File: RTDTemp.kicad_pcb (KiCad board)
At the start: 2 copper layers, 92 parts, among them J1 Conn_01x04, J10 Conn_01x04, J11 Conn_01x02, J2 Conn_01x04, J3 Conn_01x04, J4 CAN_In, J5 CAN_Out, J6 Conn_01x04, J7 Conn_01x04, J8 Conn_01x04, J9 Conn_01x04, U1 MAX31865xAP, U10 MAX31865xAP, U11 MAX31865xAP, U12 MAX31865xAP, U2 Nucleo_L432KC, U3 PDS1-Sx-Sx, U4 MAX31865xAP, U5 ADM3055E, U6 MAX31865xAP, U7 CDSOT23-T24CAN, U8 MAX31865xAP, U9 MAX31865xAP

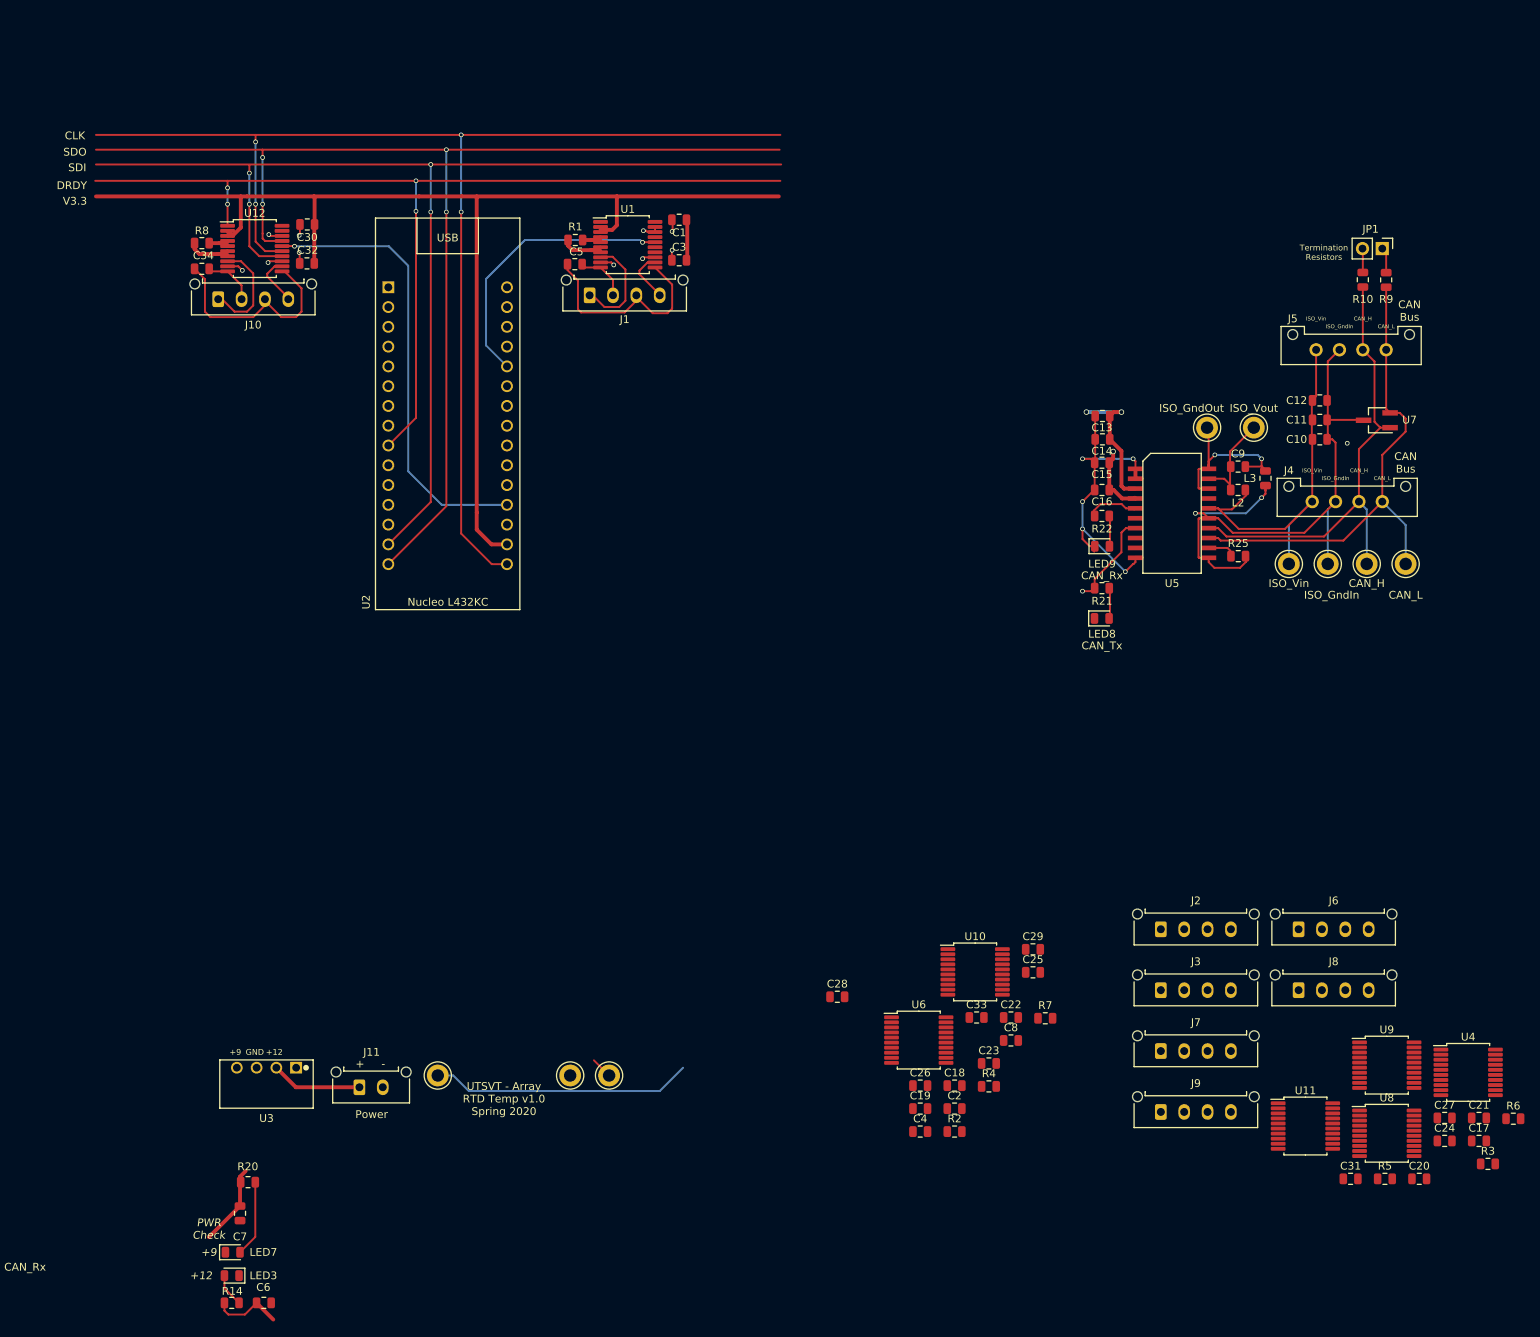
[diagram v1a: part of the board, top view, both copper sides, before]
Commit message: reset references for rtd specific components, preliminary layout of half of the RTD subcircuits
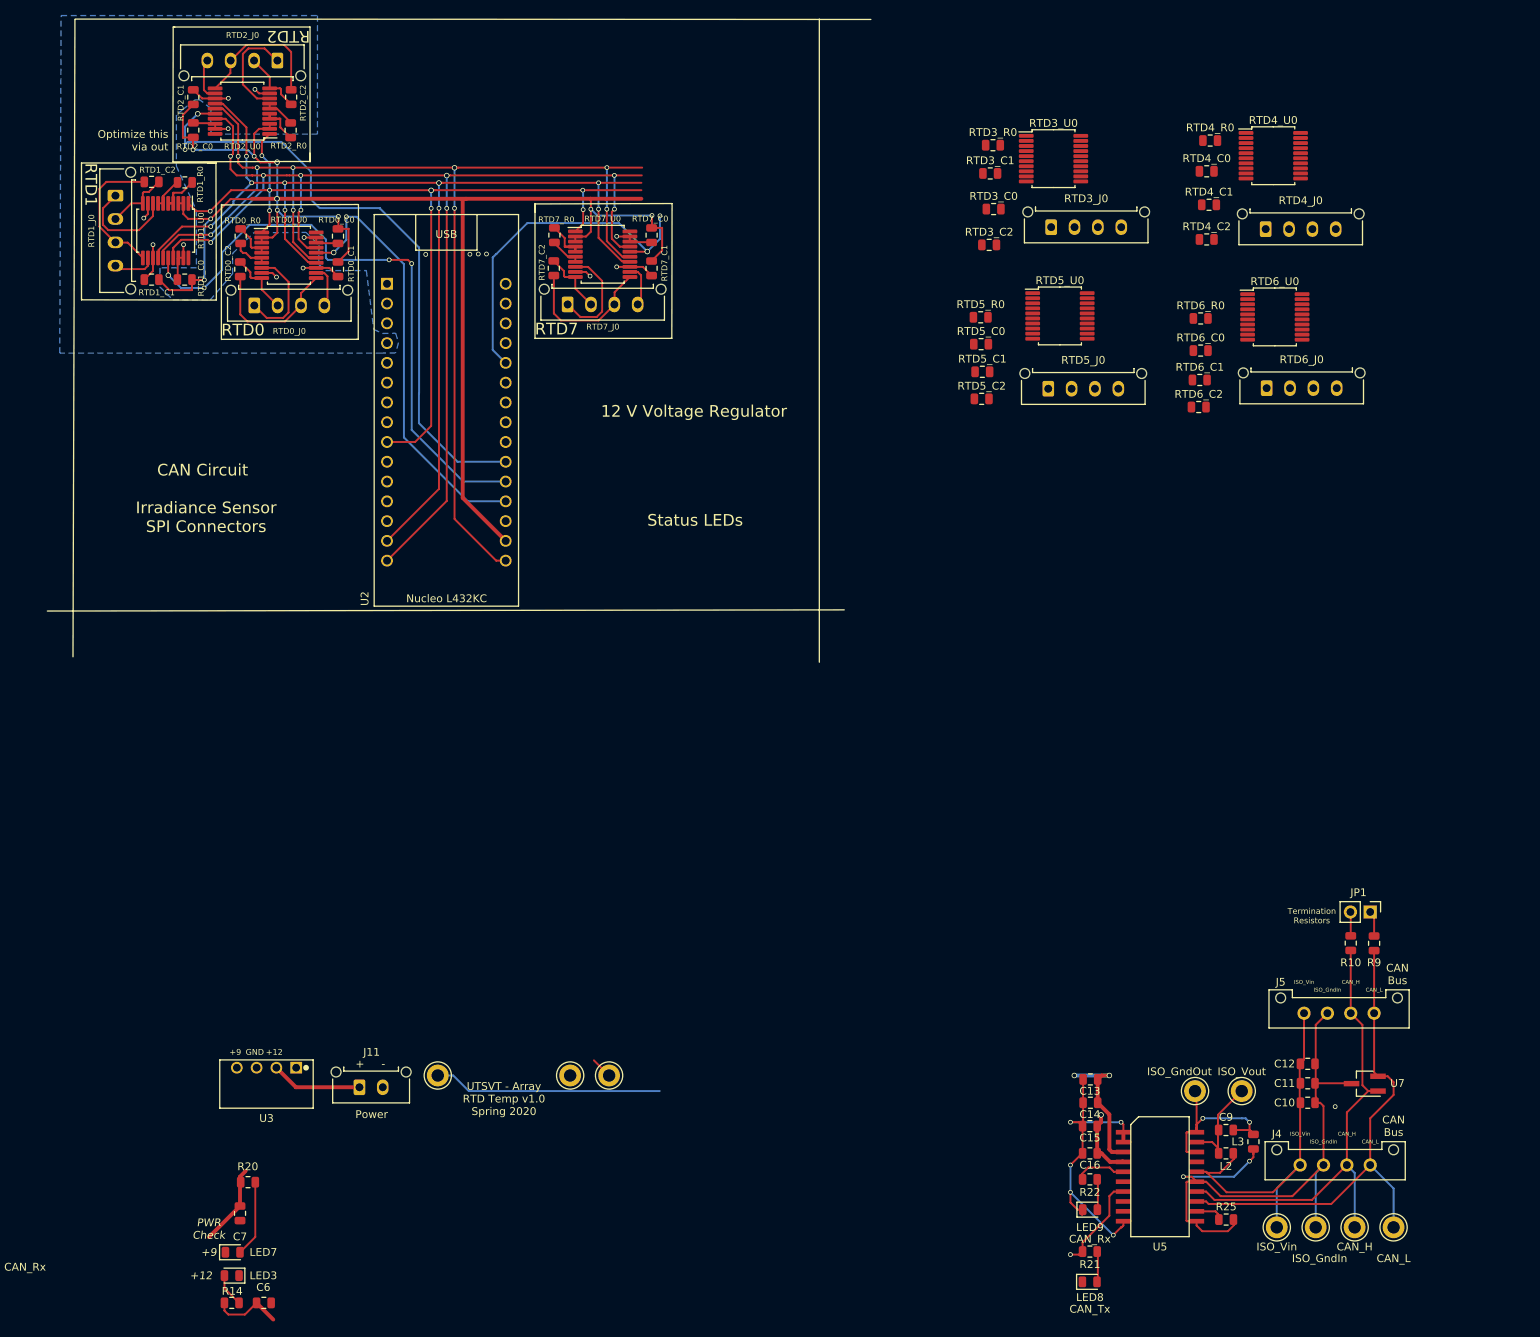
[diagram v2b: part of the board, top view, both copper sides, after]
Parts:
- removed C1, C17, C18, C19, C2, C20, C21, C22, C23, C24, C25, C26, C27, C28, C29, C3, C30, C31, C32, C33, C34, C4, C5, C8: 100nF, Capacitor_SMD:C_0805_2012Metric
- removed J1, J10, J2, J3, J6, J7, J8, J9: Conn_01x04, Connector_Molex:Molex_Micro-Fit_3.0_43650-0415_1x04_P3.00mm_Vertical
- removed R1, R2, R3, R4, R5, R6, R7, R8: 400, Resistor_SMD:R_0805_2012Metric
- removed U1, U10, U11, U12, U4, U6, U8, U9: MAX31865xAP, Package_SO:SSOP-20_5.3x7.2mm_P0.65mm
- added RTD0_C0: 100nF, Capacitor_SMD:C_0805_2012Metric, F.Cu at (127.6, 47.3)
- added RTD0_C1: 100nF, Capacitor_SMD:C_0805_2012Metric, F.Cu at (127.6, 51.6)
- added RTD0_C2: 100nF, Capacitor_SMD:C_0805_2012Metric, F.Cu at (115.1, 51.6)
- added RTD0_J0: Conn_01x04, Connector_Molex:Molex_Micro-Fit_3.0_43650-0415_1x04_P3.00mm_Vertical, F.Cu at (116.9, 56.2)
- added RTD0_R0: 400, Resistor_SMD:R_0805_2012Metric, F.Cu at (115.1, 47.3)
- added RTD0_U0: MAX31865xAP, Package_SO:SSOP-20_5.3x7.2mm_P0.65mm, F.Cu at (121.3, 49.8)
- added RTD1_C0: 100nF, Capacitor_SMD:C_0805_2012Metric, F.Cu at (107.9, 52.9)
- added RTD1_C1: 100nF, Capacitor_SMD:C_0805_2012Metric, F.Cu at (103.7, 52.9)
- added RTD1_C2: 100nF, Capacitor_SMD:C_0805_2012Metric, F.Cu at (103.7, 40.3)
- added RTD1_J0: Conn_01x04, Connector_Molex:Molex_Micro-Fit_3.0_43650-0415_1x04_P3.00mm_Vertical, F.Cu at (99.0, 42.1)
- added RTD1_R0: 400, Resistor_SMD:R_0805_2012Metric, F.Cu at (108.0, 40.4)
- added RTD1_U0: MAX31865xAP, Package_SO:SSOP-20_5.3x7.2mm_P0.65mm, F.Cu at (105.5, 46.6)
- added RTD2_C0: 100nF, Capacitor_SMD:C_0805_2012Metric, F.Cu at (109.0, 33.7)
- added RTD2_C1: 100nF, Capacitor_SMD:C_0805_2012Metric, F.Cu at (109.0, 29.5)
- added RTD2_C2: 100nF, Capacitor_SMD:C_0805_2012Metric, F.Cu at (121.6, 29.5)
- added RTD2_J0: Conn_01x04, Connector_Molex:Molex_Micro-Fit_3.0_43650-0415_1x04_P3.00mm_Vertical, F.Cu at (119.8, 24.8)
- added RTD2_R0: 400, Resistor_SMD:R_0805_2012Metric, F.Cu at (121.5, 33.7)
- added RTD2_U0: MAX31865xAP, Package_SO:SSOP-20_5.3x7.2mm_P0.65mm, F.Cu at (115.3, 31.3)
- added RTD3_C0: 100nF, Capacitor_SMD:C_0805_2012Metric, F.Cu at (211.8, 43.8)
- added RTD3_C1: 100nF, Capacitor_SMD:C_0805_2012Metric, F.Cu at (211.4, 39.3)
- added RTD3_C2: 100nF, Capacitor_SMD:C_0805_2012Metric, F.Cu at (211.3, 48.4)
- added RTD3_J0: Conn_01x04, Connector_Molex:Molex_Micro-Fit_3.0_43650-0415_1x04_P3.00mm_Vertical, F.Cu at (219.2, 46.2)
- added RTD3_R0: 400, Resistor_SMD:R_0805_2012Metric, F.Cu at (211.8, 35.6)
- added RTD3_U0: MAX31865xAP, Package_SO:SSOP-20_5.3x7.2mm_P0.65mm, F.Cu at (219.5, 37.4)
- added RTD4_C0: 100nF, Capacitor_SMD:C_0805_2012Metric, F.Cu at (239.2, 39.0)
- added RTD4_C1: 100nF, Capacitor_SMD:C_0805_2012Metric, F.Cu at (239.5, 43.3)
- added RTD4_C2: 100nF, Capacitor_SMD:C_0805_2012Metric, F.Cu at (239.2, 47.7)
- added RTD4_J0: Conn_01x04, Connector_Molex:Molex_Micro-Fit_3.0_43650-0415_1x04_P3.00mm_Vertical, F.Cu at (246.8, 46.4)
- added RTD4_R0: 400, Resistor_SMD:R_0805_2012Metric, F.Cu at (239.7, 35.0)
- added RTD4_U0: MAX31865xAP, Package_SO:SSOP-20_5.3x7.2mm_P0.65mm, F.Cu at (247.8, 37.0)
- added RTD5_C0: 100nF, Capacitor_SMD:C_0805_2012Metric, F.Cu at (210.2, 61.2)
- added RTD5_C1: 100nF, Capacitor_SMD:C_0805_2012Metric, F.Cu at (210.4, 64.7)
- added RTD5_C2: 100nF, Capacitor_SMD:C_0805_2012Metric, F.Cu at (210.3, 68.2)
- added RTD5_J0: Conn_01x04, Connector_Molex:Molex_Micro-Fit_3.0_43650-0415_1x04_P3.00mm_Vertical, F.Cu at (218.8, 66.9)
- added RTD5_R0: 400, Resistor_SMD:R_0805_2012Metric, F.Cu at (210.2, 57.7)
- added RTD5_U0: MAX31865xAP, Package_SO:SSOP-20_5.3x7.2mm_P0.65mm, F.Cu at (220.3, 57.6)
- added RTD6_C0: 100nF, Capacitor_SMD:C_0805_2012Metric, F.Cu at (238.4, 62.0)
- added RTD6_C1: 100nF, Capacitor_SMD:C_0805_2012Metric, F.Cu at (238.3, 65.8)
- added RTD6_C2: 100nF, Capacitor_SMD:C_0805_2012Metric, F.Cu at (238.2, 69.3)
- added RTD6_J0: Conn_01x04, Connector_Molex:Molex_Micro-Fit_3.0_43650-0415_1x04_P3.00mm_Vertical, F.Cu at (246.9, 66.8)
- added RTD6_R0: 400, Resistor_SMD:R_0805_2012Metric, F.Cu at (238.4, 57.9)
- added RTD6_U0: MAX31865xAP, Package_SO:SSOP-20_5.3x7.2mm_P0.65mm, F.Cu at (247.9, 57.7)
- added RTD7_C0: 100nF, Capacitor_SMD:C_0805_2012Metric, F.Cu at (167.9, 47.2)
- added RTD7_C1: 100nF, Capacitor_SMD:C_0805_2012Metric, F.Cu at (167.9, 51.5)
- added RTD7_C2: 100nF, Capacitor_SMD:C_0805_2012Metric, F.Cu at (155.3, 51.4)
- added RTD7_J0: Conn_01x04, Connector_Molex:Molex_Micro-Fit_3.0_43650-0415_1x04_P3.00mm_Vertical, F.Cu at (157.1, 56.1)
- added RTD7_R0: 400, Resistor_SMD:R_0805_2012Metric, F.Cu at (155.4, 47.2)
- added RTD7_U0: MAX31865xAP, Package_SO:SSOP-20_5.3x7.2mm_P0.65mm, F.Cu at (161.6, 49.6)
- moved J5 85.2 mm to (251.7, 147.1)
- moved JP1 85.2 mm to (260.2, 134.1)
- moved R10 85.2 mm to (257.7, 138.1)
- moved R22 85.2 mm to (224.2, 168.5)
- moved C10 85.2 mm to (252.2, 158.6)
- moved C11 85.2 mm to (252.2, 156.1)
- moved C12 85.2 mm to (252.2, 153.6)
- moved C13 85.2 mm to (224.3, 155.6)
- moved C14 85.2 mm to (224.3, 158.6)
- moved C15 85.2 mm to (224.2, 161.6)
- moved C16 85.2 mm to (224.2, 165.1)
- moved C9 85.2 mm to (241.7, 162.1)
- moved J4 85.2 mm to (251.2, 166.6)
- moved L2 85.2 mm to (241.7, 165.1)
- moved L3 85.2 mm to (245.2, 163.6)
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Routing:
- net CS_2: track 0.00 -> 81.9 mm, vias 0 -> 2
- net CS_1: track 0.00 -> 78.5 mm, vias 0 -> 4
- net +3V3: track 172.2 -> 209.6 mm, vias 1 -> 11
- net GND: track 58.8 -> 90.8 mm, vias 16 -> 18
- net Net-(C34-Pad2): track 27.9 -> 0.00 mm
- net Net-(C5-Pad2): track 27.4 -> 0.00 mm
- net Net-(RTD7_C2-Pad2): track 0.00 -> 18.2 mm
- net Net-(RTD0_C2-Pad2): track 0.00 -> 18.2 mm
- net Net-(RTD2_C2-Pad2): track 0.00 -> 18.2 mm
- net Net-(RTD1_C2-Pad2): track 0.00 -> 18.2 mm
- net Net-(J10-Pad1): track 13.5 -> 0.00 mm
- net Net-(RTD0_J0-Pad1): track 0.00 -> 13.5 mm
- net Net-(RTD2_J0-Pad1): track 0.00 -> 13.5 mm
- net Net-(RTD1_J0-Pad1): track 0.00 -> 13.5 mm
- net Net-(RTD7_J0-Pad1): track 0.00 -> 13.5 mm
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- added copper zone on B.Cu, net GND
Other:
- board text added: "12 V Voltage Regulator"
- board text added: "CAN Circuit"
- board text added: "CLK SDO SDI DRDY V3.3"
- board text added: "Irradiance Sensor SPI Connectors"
- board text added: "Optimize this via out"
- board text added: "RTD0"
- board text added: "RTD1"
- board text added: "RTD2"
- board text added: "RTD7"
- board text added: "Status LEDs"
- board text removed: "CLK"
- board text removed: "DRDY"
- board text removed: "SDI"
- board text removed: "SDO"
- board text removed: "V3.3"

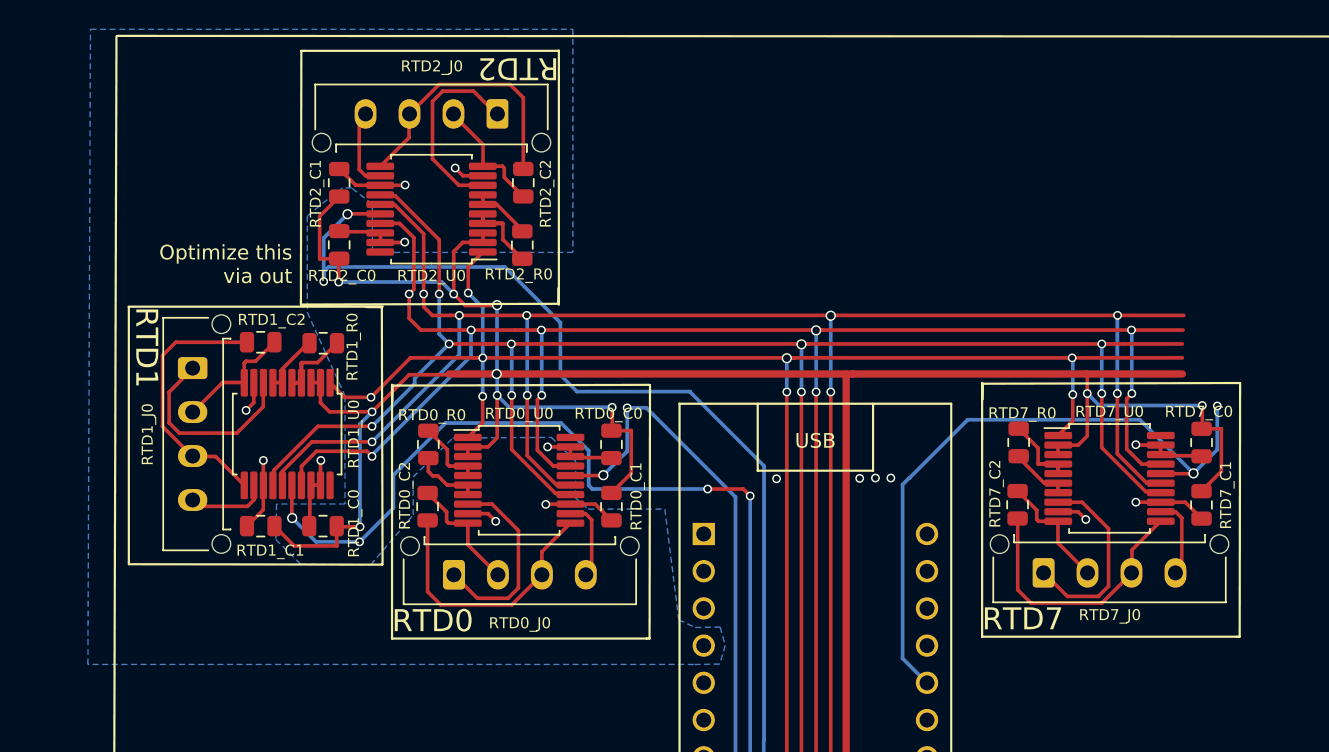
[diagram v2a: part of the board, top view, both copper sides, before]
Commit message: Updated footprints and layout
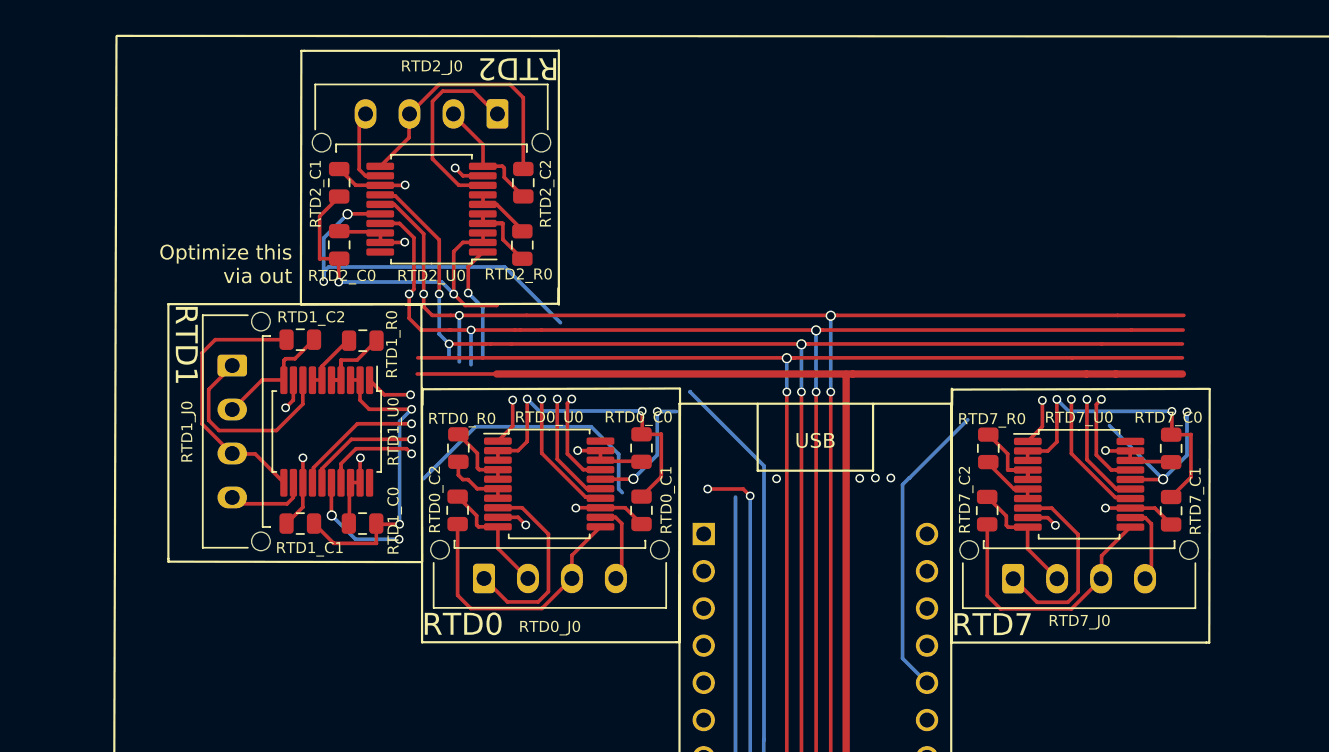
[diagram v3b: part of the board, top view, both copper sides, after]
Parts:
- moved RTD1_C0 2.71 mm to (110.6, 52.7)
- moved RTD1_C1 2.71 mm to (106.4, 52.7)
- moved RTD1_J0 2.71 mm to (101.8, 41.9)
- moved RTD1_U0 2.71 mm to (108.2, 46.4)
- moved RTD1_C2 2.71 mm to (106.4, 40.2)
- moved RTD1_R0 2.71 mm to (110.7, 40.2)
- moved RTD7_R0 2.11 mm to (153.3, 47.6)
- moved RTD7_C2 2.11 mm to (153.3, 51.8)
- moved RTD7_C0 2.11 mm to (165.8, 47.6)
- moved RTD7_C1 2.11 mm to (165.8, 51.9)
- moved RTD7_J0 2.11 mm to (155.1, 56.5)
- moved RTD7_U0 2.11 mm to (159.6, 50.0)
- moved RTD0_R0 2.07 mm to (117.2, 47.6)
- moved RTD0_C0 2.07 mm to (129.7, 47.6)
- moved RTD0_C1 2.07 mm to (129.7, 51.8)
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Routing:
- net CLK: track 160.4 -> 141.6 mm, vias 9 -> 7
- net SDO: track 158.2 -> 140.4 mm, vias 9 -> 7
- net SDI: track 153.1 -> 139.3 mm, vias 9 -> 7
- net CS_1: track 78.5 -> 65.1 mm
- net CS_2: track 81.9 -> 69.0 mm
- net CS_7: track 45.0 -> 33.2 mm
- net +3V3: track 209.6 -> 198.0 mm, vias 11 -> 9
- net DRDY: track 116.2 -> 106.8 mm, vias 8 -> 6
- net CS_0: track 56.2 -> 47.6 mm
- removed copper zone on B.Cu, net GND
